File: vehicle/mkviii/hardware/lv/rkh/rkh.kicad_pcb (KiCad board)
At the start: 2 copper layers, 118.4 x 59.2 mm, 63 parts, among them J1 TWO_WIRE_SCREW_TERMINAL, J2 TWO_WIRE_SCREW_TERMINAL, J3 TWO_WIRE_SCREW_TERMINAL, J4 TWO_WIRE_SCREW_TERMINAL, J5 VCU_pinout, J6 J_Programming_Pin_Header, J7 Conn_01x03_Pin, J8 Dashboard_PCIE, U1 STM32G441KBT6, U2 MCP2561-E-SN, U3 AP63203WU-7, Y2 X_Crystal_GND24

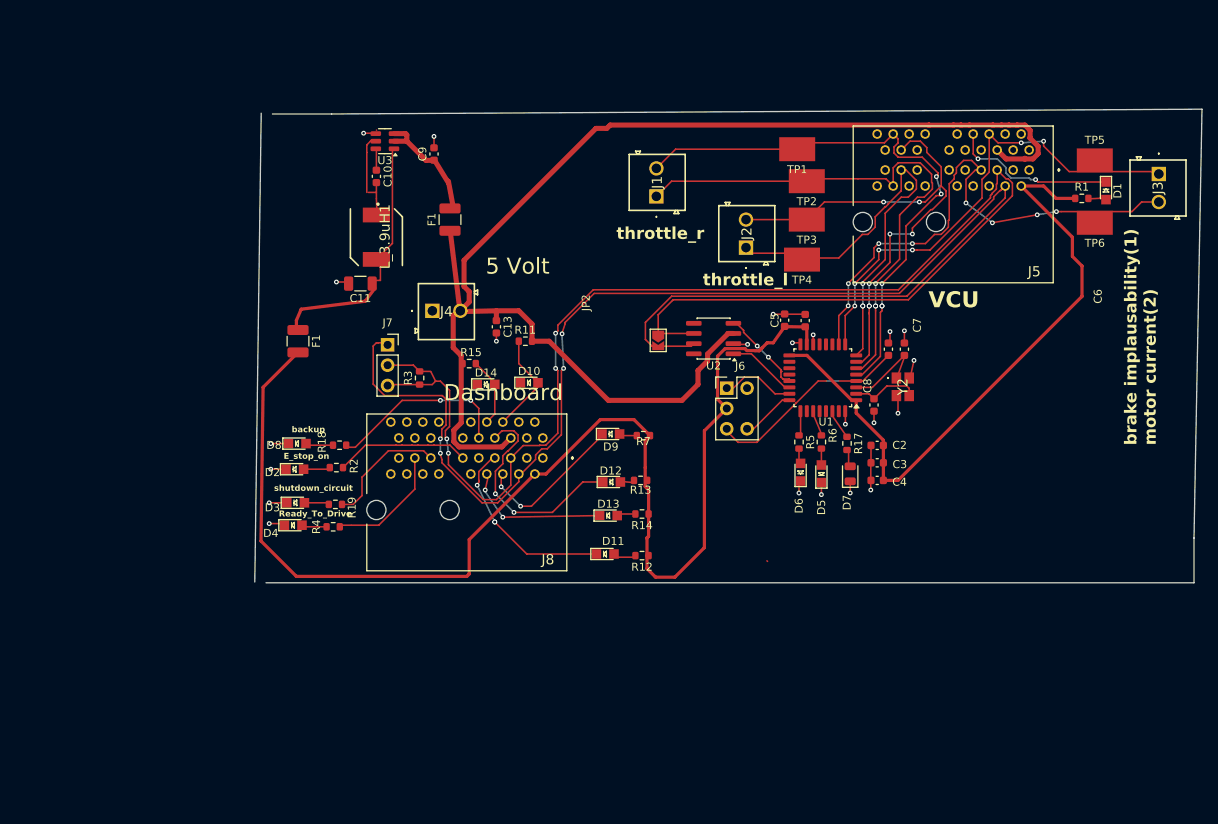
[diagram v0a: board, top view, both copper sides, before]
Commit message: RKH - routed all non CAN traces.  Still need to do DRC overview
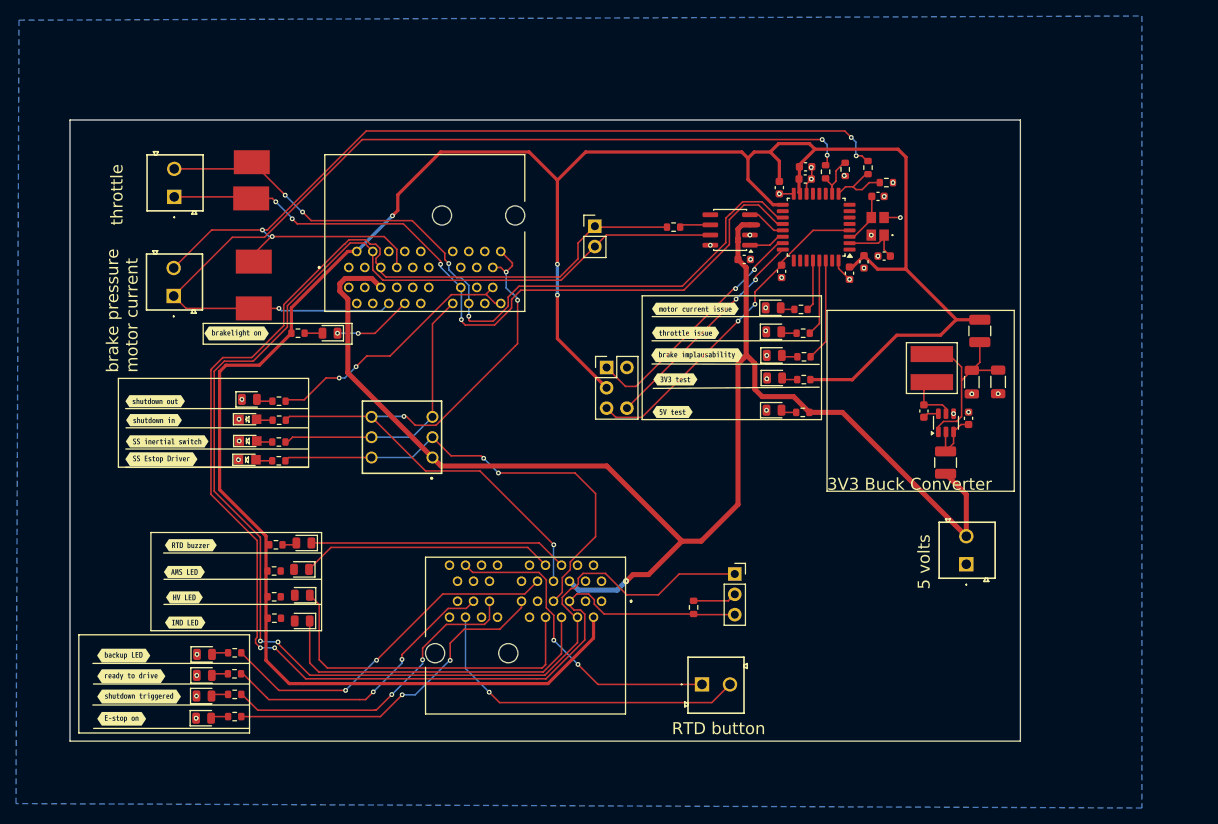
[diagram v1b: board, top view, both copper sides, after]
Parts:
- removed the F1 at (54.0, 95.0)
- removed the F1 at (73.0, 79.8)
- removed the J4 at (70.8, 91.2)
- removed J6: J_Programming_Pin_Header, OEM:J_Programming_Pin_Header_Keyed
- removed JP2: SolderJumper_2_Open, Jumper:SolderJumper-2_P1.3mm_Open_TrianglePad1.0x1.5mm
- removed R13, R14: R_1k_0.1W, OEM:R_0603_1608Metric
- removed TP5, TP6: TestPoint, OEM:Test_Point_SMD
- removed U3: AP63203WU-7, OEM:SOT-23-6
- removed Y2: X_Crystal_GND24, OEM:FA238160000MBC0 (X_16MHz_18pF_SMD - FA-238_16.0000MB-C0)
- added C12: C_22uF_25V, OEM:C_1206_3216Metric, F.Cu at (141.5, 100.1)
- added D15: LED, OEM:D_0805_2012Metric, F.Cu at (54.5, 126.8)
- added D16: LED, OEM:D_0805_2012Metric, F.Cu at (54.4, 123.5)
- added D19: LED, OEM:LED_0805_OEM, F.Cu at (47.8, 107.5)
- added D20: LED, OEM:LED_0805_OEM, F.Cu at (47.7, 104.8)
- added Dashboard_PCIE1: pcie_x1, OEM:pcie_x_delete_asap, F.Cu at (82.9, 133.0)
- added F1: Fuse, OEM:Fuse_1210_3225Metric, F.Cu at (134.9, 110.2)
- added F2: Fuse, OEM:Fuse_1210_3225Metric, F.Cu at (139.2, 93.7)
- added J4: TWO_WIRE_SCREW_TERMINAL, OEM:wire_terminal_delete_asap, F.Cu at (137.5, 122.9)
- added J4: TWO_WIRE_SCREW_TERMINAL, OEM:wire_terminal_delete_asap, F.Cu at (38.5, 89.3)
- added R10: R_120, OEM:R_0603, F.Cu at (101.0, 80.7)
- added R16: R_120k, OEM:R_0603_1608Metric, F.Cu at (103.5, 128.3)
- added R20: R_1k_0.1W, OEM:R_0603_1608Metric, F.Cu at (51.0, 127.0)
- added R21: R_1k_0.1W, OEM:R_0603_1608Metric, F.Cu at (51.0, 123.7)
- added R22: R__5k, OEM:R_0603_1608Metric, F.Cu at (125.2, 73.3)
- added R23: R_10k, OEM:R_0603_1608Metric, F.Cu at (127.5, 75.2)
- added R24: R_10k, OEM:R_0603_1608Metric, F.Cu at (122.4, 73.5)
- added R25: R__5k, OEM:R_0603_1608Metric, F.Cu at (120.0, 73.8)
- added R26: R_120, OEM:R_0603_1608Metric, F.Cu at (51.6, 104.9)
- added R8: R_1k_0.1W, OEM:R_0603_1608Metric, F.Cu at (117.2, 94.0)
- added R9: R_1k_0.1W, OEM:R_0603_1608Metric, F.Cu at (46.1, 133.9)
- added S1: DS01C-254-L-03BE, OEM:SW_DS01C254L03BE, F.Cu at (70.8, 109.5)
- added U4: MCP2561-E-SN, Package_SO:SOIC-8_3.9x4.9mm_P1.27mm, F.Cu at (108.0, 81.1)
- added Y1: Crystal_16MHz_18pF, jack_2_20_oem_copies:FA238160000MBC0 (X_16MHz_18pF_SMD - FA-238_16.0000MB-C0), F.Cu at (126.5, 80.6)
- added kibuzzard-699FC5A2: G***, kibuzzard-699FC5A2, F.Cu at (36.1, 102.5)
- added kibuzzard-699FC5B9: G***, kibuzzard-699FC5B9, F.Cu at (36.0, 104.9)
- added kibuzzard-699FC5E8: G***, kibuzzard-699FC5E8, F.Cu at (37.6, 107.5)
- added kibuzzard-699FC621: G***, kibuzzard-699FC621, F.Cu at (36.9, 109.8)
- added kibuzzard-699FCAAF: G***, kibuzzard-699FCAAF, F.Cu at (32.2, 134.3)
- added kibuzzard-699FCAF0: G***, kibuzzard-699FCAF0, F.Cu at (33.2, 136.9)
- added kibuzzard-699FCB70: G***, kibuzzard-699FCB70, F.Cu at (34.1, 139.4)
- added kibuzzard-699FCB9F: G***, kibuzzard-699FCB9F, F.Cu at (32.0, 142.2)
- added kibuzzard-699FD2AF: G***, kibuzzard-699FD2AF, F.Cu at (40.6, 120.5)
- added kibuzzard-699FD2CF: G***, kibuzzard-699FD2CF, F.Cu at (39.8, 123.8)
- added kibuzzard-699FD2EF: G***, kibuzzard-699FD2EF, F.Cu at (39.8, 127.0)
- added kibuzzard-699FD307: G***, kibuzzard-699FD307, F.Cu at (39.9, 130.2)
- added kibuzzard-699FD5DE: G***, kibuzzard-699FD5DE, F.Cu at (46.3, 94.0)
- added kibuzzard-699FD92B: G***, kibuzzard-699FD92B, F.Cu at (103.7, 91.0)
- added kibuzzard-699FD93E: G***, kibuzzard-699FD93E, F.Cu at (102.5, 94.0)
- added kibuzzard-699FD955: G***, kibuzzard-699FD955, F.Cu at (103.9, 96.8)
- added kibuzzard-699FD9DF: G***, kibuzzard-699FD9DF, F.Cu at (101.2, 99.8)
- added kibuzzard-699FD9F6: G***, kibuzzard-699FD9F6, F.Cu at (100.8, 103.8)
- C1: value C_10nF_50V -> C_10uF_10V
- C11: value C_22uF_25V -> C_10nF_50V; footprint OEM:C_1206_3216Metric -> OEM:C_0603_1608Metric
- C13: footprint OEM:C_0603_1608Metric -> OEM:C_0603
- C2: value C_0.47uF_25V -> C_0.1uF_16V
- C3: value C_0.1uF_16V -> C_22uF_25V; footprint OEM:C_0603_1608Metric -> OEM:C_1206_3216Metric
- C7: value 30pf -> 30pF
- C9: value C_10uF_10V -> C_4.7uF_25V
- D1, D10, D12, D13, D14, D2, D3, D4, D8, D9: footprint OEM:LED_0805_OEM -> OEM:D_0805_2012Metric
- D5: value LED_Motor_Current_Issue_If_On -> LED; footprint OEM:LED_0805_OEM -> OEM:D_0805_2012Metric
- D6: value LED_break_implausability_if_on -> LED; footprint OEM:LED_0805_OEM -> OEM:D_0805_2012Metric
- D7: value LED_Throttle_Issue_If_On -> LED
- J1, J2: footprint OEM:TAD05021LG -> OEM:wire_terminal_delete_asap
- J3: value TWO_WIRE_SCREW_TERMINAL -> J_PCIe_x1; footprint OEM:TAD05021LG -> OEM:pcie_x_delete_asap
- J5: value VCU_pinout -> J_Programming_Pin_Header; footprint OEM:J_PCIe_x1 -> jack_2_20_oem_copies:J_Programming_Pin_Header_Keyed
- J8: value Dashboard_PCIE -> Conn_01x02_Pin; footprint OEM:J_PCIe_x1 -> Connector_PinHeader_2.54mm:PinHeader_1x02_P2.54mm_Vertical
- L_3.9uH1: footprint OEM:SPM6530 (L_2.2uH_8.2A_19m_SMD - SPM6530T-2R2M) -> OEM:IND_BOURNS_SRR5018 (L_3.9uH_2A_55m_SMD)
- R19: value R_1k_0.1W -> R_5k
- TP1, TP2, TP3, TP4: footprint OEM:Test_Point_SMD -> OEM:test_point_delete_asap
- U1: value STM32G441KBT6 -> AP63203WU-7; footprint OEM:LQFP-32_7x7mm_P0.8mm -> OEM:SOT-23-6
- U2: value MCP2561-E-SN -> Roadkill_MCU; footprint Package_SO:SOIC-8_3.9x4.9mm_P1.27mm -> OEM:LQFP-32_7x7mm_P0.8mm
- moved R1 99.4 mm to (54.0, 94.0)
- moved D1 98.6 mm to (58.0, 94.0), turned to 180 degrees
- moved J3 92.5 mm to (69.3, 80.3), turned to 180 degrees
- moved J2 71.8 mm to (38.5, 77.0)
- moved L_3.9uH1 71.3 mm to (133.2, 98.4), turned to 90 degrees
- moved TP1 70.9 mm to (48.5, 91.4)
- moved TP2 69.9 mm to (48.5, 85.5)
- moved TP3 69.7 mm to (48.2, 73.1)
- moved TP4 69.2 mm to (48.1, 77.7)
- moved J1 61.3 mm to (104.5, 137.9), turned to 0 degrees
- moved C10 60.4 mm to (122.9, 86.5), turned to 90 degrees
- moved R18 58.6 mm to (117.2, 99.8), turned to 0 degrees
- moved J5 58.3 mm to (92.6, 98.3)
- moved C11 57.1 mm to (117.4, 74.7), turned to 0 degrees
- moved C9 55.4 mm to (124.8, 85.1), turned to -90 degrees
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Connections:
- C1 pad 1: +3V3 -> Net-(U1-EN)
- C10 pad 1: Net-(U3-BST) -> GND
- C10 pad 2: Net-(U3-SW) -> +3.3V
- C11 pad 1: +3V3 -> +3.3V
- C2 pad 1: +3V3 -> Net-(U1-BST)
- C2 pad 2: GND -> Net-(U1-SW)
- C3 pad 1: GND -> Net-(U1-FB)
- C3 pad 2: +3V3 -> GND
- C4 pad 2: +3V3 -> +3.3V
- C5 pad 1: +3V3 -> +3.3V
- C7 pad 1: Net-(U1-PF1-OSC_OUT) -> Net-(U2-PF1-OSC_OUT)
- C8 pad 1: Net-(U1-PF0-OSC_IN) -> Net-(U2-PF0-OSC_IN)
- C9 pad 1: +5V -> +3.3V
- D1 pad 1: Net-(D1-K) -> /BRAKE_LIGHT
- D10 pad 1: Net-(D10-K) -> GND
- D11 pad 1: Net-(D11-K) -> GND
- D12 pad 1: Net-(D12-K) -> /RTD_BUZZER_LOW_SIDE
- D13 pad 1: unconnected-(D13-K-Pad1) -> GND
- D14 pad 1: Net-(D14-K) -> GND
- D9 pad 1: Net-(D9-K) -> /IMD_LED_LOW_SIDE
- J1 pad 1: /throttle_r+ -> Net-(Dashboard_PCIE1-io_21)
- J1 pad 2: /throttle_r- -> Net-(Dashboard_PCIE1-io_20)
- J2 pad 1: /throttle_l+ -> /THROTTLE_L+
- J2 pad 2: /throttle_l- -> /THROTTLE_R+
- J7 pad 2: /CAN_- -> Net-(J7-Pin_2)
- L_3.9uH1 pad 1: Net-(U3-SW) -> Net-(U1-SW)
- L_3.9uH1 pad 2: +3V3 -> Net-(U1-FB)
- R1 pad 1: +3V3 -> +3.3V
- R11 pad 1: +5V -> +3.3V
- R11 pad 2: Net-(D10-A) -> Net-(D12-A)
- R12 pad 1: +3V3 -> Net-(D11-A)
- R12 pad 2: Net-(D11-A) -> /SS_ESTOP_DRIVER
- R15 pad 1: +5V -> Net-(D14-A)
- R15 pad 2: Net-(D14-A) -> /SHDN_OUT_VCU
- R17 pad 1: Net-(D7-A) -> Net-(D10-A)
- R17 pad 2: Net-(U1-(TIM3_CH4/TIM4_CH2/TIM17_CH1N/GPIO_EXTI7)PB7) -> +5V
- R18 pad 1: Net-(J8-io_7) -> Net-(D13-A)
- R18 pad 2: Net-(D8-A) -> +3.3V
- R19 pad 1: /shutdown_circuit_triggered -> Net-(D19-A)
- R19 pad 2: Net-(D3-A) -> /SS_INERTIA_SWITCH
- R2 pad 1: /E_stop_on -> /E_STOP_ON
- R3 pad 1: /CAN_- -> /SHUTDOWN_CIRCUIT_TRIGGERED
- R3 pad 2: /CAN_- -> Net-(D3-A)
- R4 pad 1: /Ready_to_drive -> /READY_TO_DRIVE
- R5 pad 2: Net-(U1-(TIM2_ETR/TIM2_CH1/GPIO_EXTI15)PA15) -> /BRAKE_IMPLAUSABILITY
- R6 pad 2: Net-(U1-(TIM17_BKIN/SPI1_MISO/TIM3_CH1/TIM16_CH1/GPIO_EXTI4)PB4) -> /MOTOR_CURRENT_ISSUE
- R7 pad 1: +3V3 -> +3.3V
- TP1 pad 1: /throttle_r- -> /BRAKE_PRESSURE
- TP2 pad 1: /throttle_r+ -> /MOTOR_CURRENT
- TP3 pad 1: /throttle_l- -> /THROTTLE_R+
- TP4 pad 1: /throttle_l+ -> /THROTTLE_L+
- U1 pad 1: +3V3 -> Net-(U1-FB)
- U1 pad 2: Net-(U1-PF0-OSC_IN) -> Net-(U1-EN)
- U1 pad 3: Net-(U1-PF1-OSC_OUT) -> Net-(U1-EN)
- U1 pad 4: /NRST -> GND
- U1 pad 5: /throttle_r- -> Net-(U1-SW)
- U1 pad 6: /throttle_r+ -> Net-(U1-BST)
- U2 pad 1: /CAN_TX -> +3.3V
- U2 pad 2: GND -> Net-(U2-PF0-OSC_IN)
- U2 pad 3: +5V -> Net-(U2-PF1-OSC_OUT)
- U2 pad 4: /CAN_RX -> /NRST
- U2 pad 6: /CAN_- -> unconnected-(U2-(TIM15_CH1N/TIM2_CH2/GPIO_EXTI1/ADC2_IN2/ADC1_IN2)PA1*-Pad6)
- U2 pad 7: /CAN_+ -> unconnected-(U2-(TIM15_CH1/USART2_TX/TIM2_CH3/GPIO_EXTI2/ADC1_IN3)PA2*-Pad7)
- U2 pad 8: GND -> unconnected-(U2-(TIM15_CH2/USART2_RX/TIM2_CH4/GPIO_EXTI3/ADC1_IN4)PA3*-Pad8)
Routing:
- net +3.3V: track 0.00 -> 293.2 mm, vias 0 -> 3
- net +3V3: track 243.3 -> 0.00 mm
- net /MOTOR_CURRENT: track 0.00 -> 120.9 mm, vias 0 -> 4
- net /BRAKE_PRESSURE: track 0.00 -> 120.9 mm, vias 0 -> 3
- net /THROTTLE_R+: track 0.00 -> 97.6 mm, vias 0 -> 4
- net /THROTTLE_L+: track 0.00 -> 95.4 mm, vias 0 -> 4
- net /SHDN_IN_VCU: track 0.00 -> 83.2 mm, vias 0 -> 4
- net /throttle_r-: track 65.5 -> 0.00 mm, vias 5 -> 0
- net /throttle_r+: track 62.5 -> 0.00 mm, vias 3 -> 0
- net /SS_ESTOP_DRIVER: track 0.00 -> 58.5 mm, vias 0 -> 2
- net /throttle_l-: track 53.2 -> 0.00 mm, vias 7 -> 0
- net /throttle_l+: track 50.6 -> 0.00 mm, vias 3 -> 0
- net /break_pressure_sensor: track 50.2 -> 0.00 mm, vias 6 -> 0
- net /motor_current_sense: track 45.4 -> 0.00 mm, vias 8 -> 0
- net /BACKUP_LED: track 0.00 -> 44.6 mm, vias 0 -> 2
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- added copper zone on B.Cu, net GND
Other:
- board size 118.4 x 59.2 mm -> 118.8 x 77.6 mm
- board text added: "3V3 Buck Converter"
- board text added: "5 volts"
- board text added: "RTD button"
- board text added: "brake pressure motor current"
- board text added: "throttle"
- board text removed: "5 Volt"
- board text removed: "AP63203WU-7"
- board text removed: "Brake_Implausability"
- board text removed: "C6"
- board text removed: "Dashboard"
- board text removed: "E_stop_on"
- board text removed: "JP2"
- board text removed: "Motor_current"
- board text removed: "R18"
- board text removed: "Ready_To_Drive"
- board text removed: "VCU"
- board text removed: "backup"
- board text removed: "brake implausability(1) motor current(2)"
- board text removed: "shutdown_circuit"
- board text removed: "throttle_l"
- board text removed: "throttle_r"

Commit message: rkh: Layout for review
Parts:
- added kibuzzard-69A0E477: G***, kibuzzard-69A0E477, F.Cu at (80.9, 94.7)
- added kibuzzard-69A0E4A7: G***, kibuzzard-69A0E4A7, F.Cu at (75.3, 118.3)
- moved D9 0.50 mm to (54.5, 129.5)
- moved R7 0.06 mm to (51.0, 129.7)
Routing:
- net GND: track 10.4 -> 18.6 mm
- net +3.3V: track 293.2 -> 295.3 mm
- net Net-(D15-A): track 0.00 -> 1.83 mm
- net Net-(D9-A): track 0.00 -> 1.82 mm
- net Net-(D16-A): track 0.00 -> 1.75 mm

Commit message: RKH - ready to review!  planes added!
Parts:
- removed kibuzzard-699FC5A2: G***, kibuzzard-699FC5A2
- removed kibuzzard-699FC5B9: G***, kibuzzard-699FC5B9
- removed kibuzzard-699FC5E8: G***, kibuzzard-699FC5E8
- removed kibuzzard-699FC621: G***, kibuzzard-699FC621
- added kibuzzard-69A764DF: G***, kibuzzard-69A764DF, F.Cu at (131.8, 119.3)
- added kibuzzard-69A764E7: G***, kibuzzard-69A764E7, F.Cu at (131.5, 123.0)
- added kibuzzard-69A764F6: G***, kibuzzard-69A764F6, F.Cu at (112.0, 136.2)
- added kibuzzard-69A764F6: G***, kibuzzard-69A764F6, F.Cu at (112.0, 140.9)
- added kibuzzard-69A76600: G***, kibuzzard-69A76600, F.Cu at (31.6, 72.9)
- added kibuzzard-69A76676: G***, kibuzzard-69A76676, F.Cu at (31.8, 77.7)
- added kibuzzard-69A766BA: G***, kibuzzard-69A766BA, F.Cu at (31.2, 85.2)
- added kibuzzard-69A76791: G***, kibuzzard-69A76791, F.Cu at (30.9, 90.0)
- added kibuzzard-69AA1B51: G***, kibuzzard-69AA1B51, F.Cu at (34.3, 105.0)
- added kibuzzard-69AA1B5D: G***, kibuzzard-69AA1B5D, F.Cu at (34.1, 102.5)
- added kibuzzard-69AA3EC3: G***, kibuzzard-69AA3EC3, F.Cu at (36.9, 107.6)
- added kibuzzard-69AA3EDE: G***, kibuzzard-69AA3EDE, F.Cu at (36.3, 109.8)
- moved J4 1.57 mm to (40.0, 89.3)
- moved J1 1.51 mm to (104.9, 136.4), turned to -90 degrees
- moved J2 1.45 mm to (40.0, 76.9)
- moved C4 1.12 mm to (113.4, 76.6), turned to 180 degrees
- moved TP3 0.68 mm to (48.2, 72.5)
- moved TP4 0.67 mm to (47.9, 78.3)
- moved kibuzzard-699FD307 0.47 mm to (39.8, 129.7)
- moved kibuzzard-699FCB9F 0.42 mm to (32.0, 141.8)
- moved kibuzzard-699FD9DF 0.29 mm to (101.0, 100.0)
- moved kibuzzard-699FD2EF 0.20 mm to (39.6, 127.0)
- moved kibuzzard-699FD955 0.14 mm to (104.0, 96.8)
- moved kibuzzard-699FD2AF 0.13 mm to (40.5, 120.5)
- moved D2 0.13 mm to (42.2, 142.0)
- moved kibuzzard-69A0E4A7 0.13 mm to (75.5, 118.4)
- moved kibuzzard-699FD9F6 0.08 mm to (100.8, 103.9)
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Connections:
- R10 pad 1: /CAN_- -> /CAN_+
- R10 pad 2: Net-(U4-CANL) -> /CAN_-
- U4 pad 6: Net-(U4-CANL) -> /CAN_-
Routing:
- net +3.3V: track 295.3 -> 283.1 mm
- net /CAN_-: track 181.5 -> 187.1 mm
- net Net-(U4-CANL): track 3.88 -> 0.00 mm
- net Net-(Dashboard_PCIE1-io_20): track 42.2 -> 39.0 mm
- net /BRAKE_PRESSURE: track 120.9 -> 117.7 mm
- net +5V: track 179.7 -> 176.8 mm
- net /MOTOR_CURRENT: track 120.9 -> 118.7 mm
- net /THROTTLE_L+: track 95.4 -> 94.2 mm
- net /THROTTLE_R+: track 97.6 -> 96.6 mm
- net Net-(U1-FB): track 23.7 -> 22.9 mm, vias 0 -> 2
- net /SHDN_IN_VCU: track 83.2 -> 82.5 mm
- added copper zone on F.Cu, net GND
- added copper zone on F.Cu, net Net-(U1-EN)
- added copper zone on F.Cu, net Net-(U1-FB)
- added copper zone on F.Cu, net Net-(U1-SW)
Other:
- board text added: "BP"
- board text added: "CAN"
- board text added: "CAN terminal"
- board text added: "MC"
- board text added: "Roadkill Harness Jack Goode"
- board text added: "TL"
- board text added: "TR"
- board text removed: "5 volts"
- board text removed: "RTD button"
- board text removed: "brake pressure motor current"
- board text removed: "throttle"

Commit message: Added production files; rounded corners; added throttle power wire terminal
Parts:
- added J6: TWO_WIRE_SCREW_TERMINAL, OEM:wire_terminal_delete_asap, F.Cu at (37.5, 99.3)
- added REF**: OEM_Logo_8mm, OEM:OEM_Logo_8mm, B.Cu at (139.3, 72.3)
- added TP5: TP_SMD, OEM:TP_Hook_SMD, F.Cu at (115.8, 124.6)
- added TP6: TP_SMD, OEM:TP_Hook_SMD, F.Cu at (115.8, 128.6)
- added TP7: TP_SMD, OEM:TP_Hook_SMD, F.Cu at (125.7, 119.2)
- added TP8: TP_SMD, OEM:TP_Hook_SMD, F.Cu at (139.7, 88.4)
- added TP9: TP_SMD, OEM:TP_Hook_SMD, F.Cu at (125.7, 123.2)
- added kibuzzard-69B8BF7C: G***, kibuzzard-69B8BF7C, F.Cu at (29.7, 99.7)
- added kibuzzard-69B8BF88: G***, kibuzzard-69B8BF88, F.Cu at (29.9, 95.5)
- added kibuzzard-69B8C0D1: G***, kibuzzard-69B8C0D1, B.Cu at (125.4, 69.5)
- added kibuzzard-69B8C11E: G***, kibuzzard-69B8C11E, B.Cu at (130.9, 72.3)
- added kibuzzard-69B8C173: G***, kibuzzard-69B8C173, B.Cu at (128.8, 75.2)
- moved D11 3.00 mm to (47.6, 112.8)
- moved D14 3.00 mm to (47.9, 105.3)
- moved D19 3.00 mm to (47.8, 110.5)
- moved D20 3.00 mm to (47.7, 107.8)
- moved R12 3.00 mm to (51.6, 113.0)
- moved R15 3.00 mm to (51.6, 105.5)
- moved R19 3.00 mm to (51.6, 110.6)
- moved R26 3.00 mm to (51.6, 107.9)
- moved S1 3.00 mm to (70.8, 112.5)
- moved kibuzzard-69AA1B51 3.00 mm to (34.3, 108.0)
- moved kibuzzard-69AA1B5D 3.00 mm to (34.1, 105.5)
- moved kibuzzard-69AA3EC3 3.00 mm to (36.9, 110.6)
- moved kibuzzard-69AA3EDE 3.00 mm to (36.3, 112.8)
- renumbered J4 to J9
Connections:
- J3 pad B10: unconnected-(J3-io_9-PadB10) -> /THROTTLE_POWER_L
- J3 pad B11: unconnected-(J3-io_11-PadB11) -> /THROTTLE_POWER_R
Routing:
- net /THROTTLE_POWER_R: track 0.00 -> 38.9 mm, vias 0 -> 4
- net /THROTTLE_POWER_L: track 0.00 -> 36.2 mm, vias 0 -> 4
- net +5V: track 176.8 -> 193.4 mm, vias 1 -> 2
- net /SS_ESTOP_DRIVER: track 58.5 -> 49.1 mm, vias 2 -> 0
- net /CAN_-: track 187.1 -> 194.5 mm
- net /CAN_+: track 184.9 -> 192.4 mm
- net +3.3V: track 283.1 -> 287.2 mm
- net /SS_INERTIA_SWITCH: track 35.0 -> 38.0 mm, vias 0 -> 1
- net /SHDN_OUT_VCU: track 34.1 -> 36.1 mm
- net /SHDN_IN_VCU: track 82.5 -> 81.6 mm
- net GND: vias 32 -> 33
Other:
- outline, holes or cut-outs redrawn
- board text added: "3.3 V"
- board text added: "5V"
- board text added: "CAN+"
- board text added: "CAN-"
- board text added: "GND"
